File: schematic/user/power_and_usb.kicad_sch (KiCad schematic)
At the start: 39 parts, among them J1 TYPE-C-31-M-04, Q1 AO3401A, Q2 AO3401A, Q5 MBT3904DW1T1, U1 TP4056, U2 MAX17048G+T10, U3 NCP167AFCT330T2G, U6 ESD122DMXR

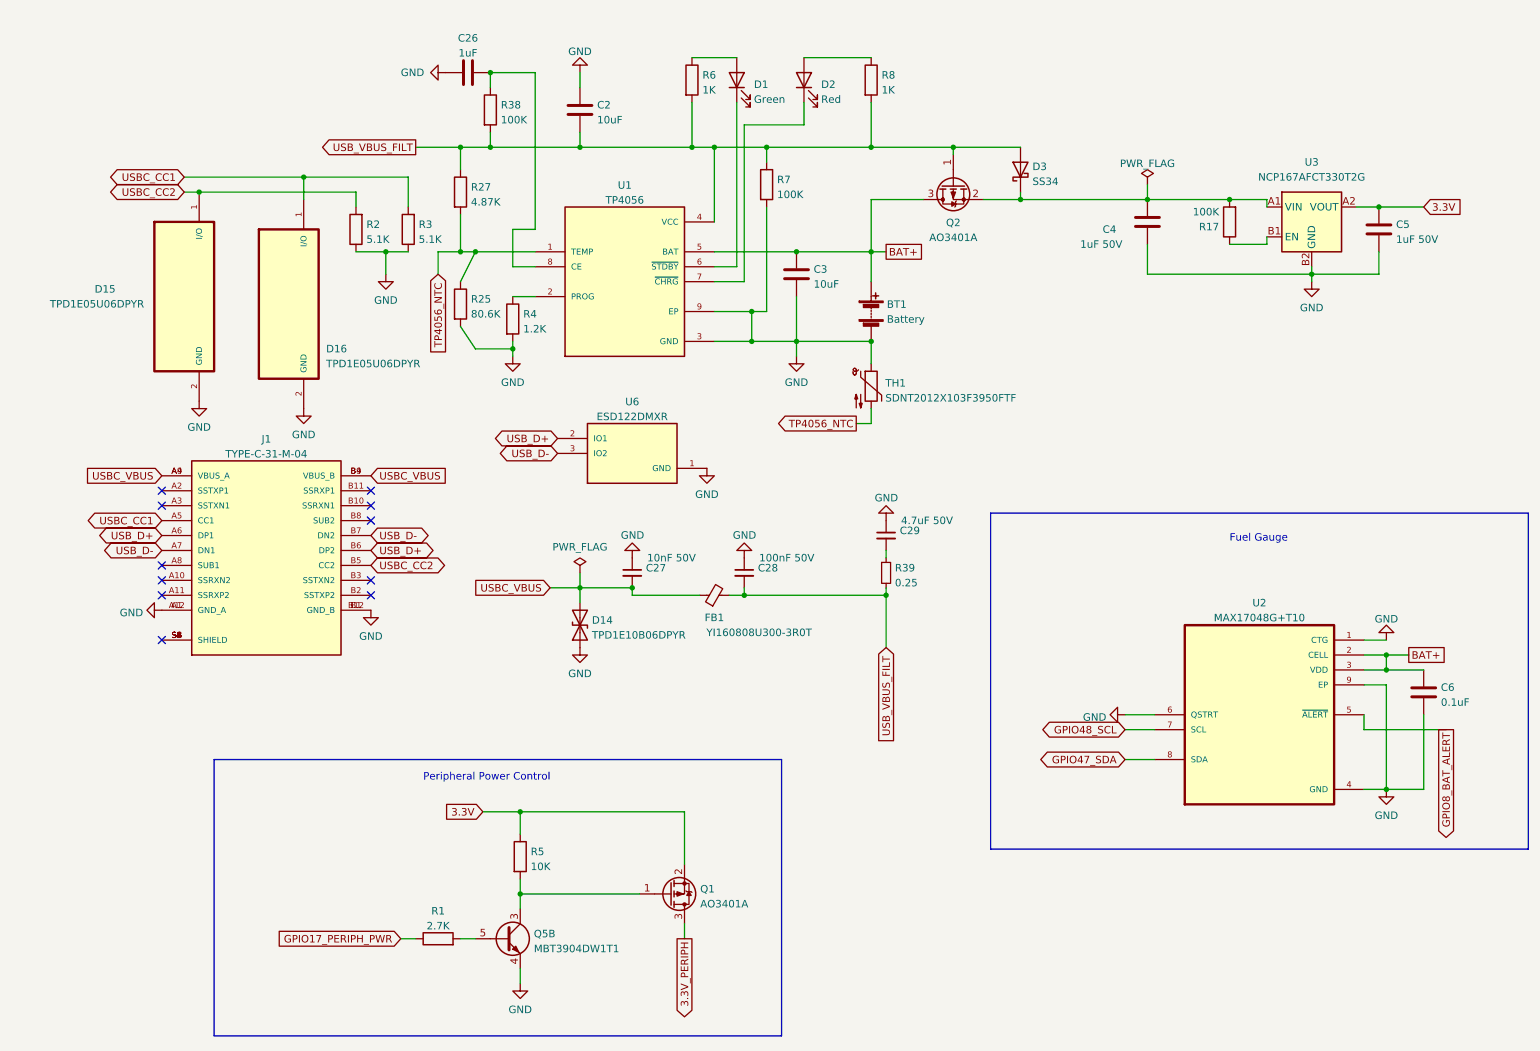
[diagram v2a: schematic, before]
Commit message: v0.7 board: resolve all ERC errors in schematic.
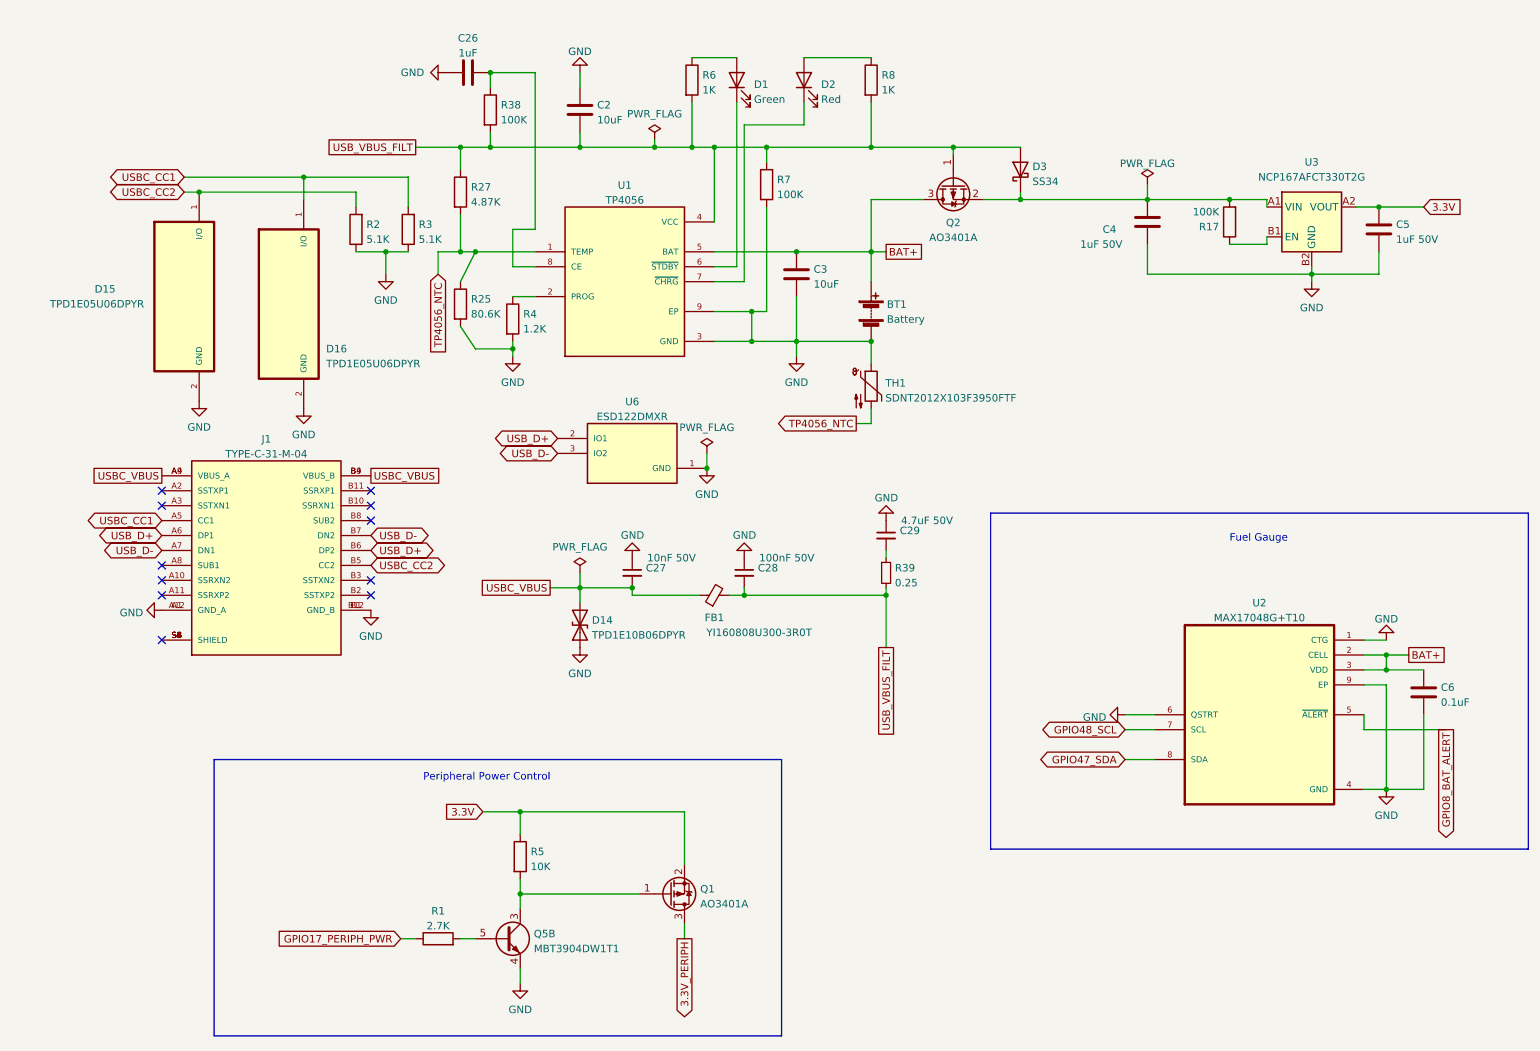
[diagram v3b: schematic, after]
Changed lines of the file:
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@@
   (junction (at 254 144.78) (diameter 0) (color 0 0 0 0)
   )
+  (junction (at 138.43 90.17) (diameter 0) (color 0 0 0 0)
+  )
   (junction (at 153.67 68.58) (diameter 0) (color 0 0 0 0)
   )
@@
   )
   (junction (at 191.77 44.45) (diameter 0) (color 0 0 0 0)
+  )
+  (junction (at 129.54 35.56) (diameter 0) (color 0 0 0 0)
   )
   (junction (at 146.05 63.5) (diameter 0) (color 0 0 0 0)
@@
     (stroke (width 0) (type default) (color 0 0 0 0))
   )
+  (wire (pts (xy 166.37 53.34) (xy 166.37 58.42))
+    (stroke (width 0) (type default) (color 0 0 0 0))
+  )
   (wire (pts (xy 105.41 49.53) (xy 105.41 55.88))
     (stroke (width 0) (type default) (color 0 0 0 0))
@@
     (stroke (width 0) (type default) (color 0 0 0 0))
   )
-  (wire (pts (xy 116.84 35.56) (xy 135.89 35.56))
+  (wire (pts (xy 116.84 35.56) (xy 129.54 35.56))
     (stroke (width 0) (type default) (color 0 0 0 0))
   )
@@
     (stroke (width 0) (type default) (color 0 0 0 0))
   )
-  (wire (pts (xy 166.37 53.34) (xy 166.37 58.42))
-    (stroke (width 0) (type default) (color 0 0 0 0))
-  )
   (wire (pts (xy 153.67 68.58) (xy 153.67 60.96))
     (stroke (width 0) (type default) (color 0 0 0 0))
@@
     (stroke (width 0) (type default) (color 0 0 0 0))
   )
+  (wire (pts (xy 129.54 34.29) (xy 129.54 35.56))
+    (stroke (width 0) (type default) (color 0 0 0 0))
+  )
   (wire (pts (xy 49.53 40.64) (xy 69.85 40.64))
     (stroke (width 0) (type default) (color 0 0 0 0))
@@
     (stroke (width 0) (type default) (color 0 0 0 0))
   )
+  (wire (pts (xy 138.43 87.63) (xy 138.43 90.17))
+    (stroke (width 0) (type default) (color 0 0 0 0))
+  )
   (wire (pts (xy 254 144.78) (xy 260.35 144.78))
     (stroke (width 0) (type default) (color 0 0 0 0))
@@
   )
   (wire (pts (xy 166.37 27.94) (xy 166.37 35.56))
+    (stroke (width 0) (type default) (color 0 0 0 0))
+  )
+  (wire (pts (xy 129.54 35.56) (xy 135.89 35.56))
     (stroke (width 0) (type default) (color 0 0 0 0))
   )
@@
     )
   )
-  (global_label "USBC_VBUS" (shape input) (at 81.28 91.44 0) (fields_autoplaced)
+  (global_label "USBC_VBUS" (shape passive) (at 81.28 91.44 0) (fields_autoplaced)
     (effects (font (size 1.27 1.27)) (justify left))
     (property "Intersheet References" "${INTERSHEET_REFS}" (id 0) (at 94.6393 91.3606 0)
@@
     )
   )
-  (global_label "USBC_VBUS" (shape input) (at 111.76 110.49 180) (fields_autoplaced)
-    (effects (font (size 1.27 1.27)) (justify right))
-    (property "Intersheet References" "${INTERSHEET_REFS}" (id 0) (at 98.4007 110.5694 0)
-      (effects (font (size 1.27 1.27)) (justify right) hide)
-    )
-  )
-  (global_label "USB_VBUS_FILT" (shape input) (at 168.91 120.65 270) (fields_autoplaced)
-    (effects (font (size 1.27 1.27)) (justify right))
-    (property "Intersheet References" "${INTERSHEET_REFS}" (id 0) (at 168.9894 137.396 90)
+  (global_label "USBC_VBUS" (shape passive) (at 111.76 110.49 180) (fields_autoplaced)
+    (effects (font (size 1.27 1.27)) (justify right))
+    (property "Intersheet References" "${INTERSHEET_REFS}" (id 0) (at 98.4007 110.4106 0)
+      (effects (font (size 1.27 1.27)) (justify right) hide)
+    )
+  )
+  (global_label "USB_VBUS_FILT" (shape passive) (at 168.91 120.65 270) (fields_autoplaced)
+    (effects (font (size 1.27 1.27)) (justify right))
+    (property "Intersheet References" "${INTERSHEET_REFS}" (id 0) (at 168.8306 137.396 90)
       (effects (font (size 1.27 1.27)) (justify right) hide)
     )
@@
     )
   )
-  (global_label "USB_VBUS_FILT" (shape output) (at 88.9 35.56 180) (fields_autoplaced)
+  (global_label "USB_VBUS_FILT" (shape passive) (at 88.9 35.56 180) (fields_autoplaced)
     (effects (font (size 1.27 1.27)) (justify right))
     (property "Intersheet References" "${INTERSHEET_REFS}" (id 0) (at 72.154 35.4806 0)
@@
     )
   )
-  (global_label "USBC_VBUS" (shape input) (at 45.72 91.44 180) (fields_autoplaced)
-    (effects (font (size 1.27 1.27)) (justify right))
-    (property "Intersheet References" "${INTERSHEET_REFS}" (id 0) (at 32.3607 91.5194 0)
+  (global_label "USBC_VBUS" (shape passive) (at 45.72 91.44 180) (fields_autoplaced)
+    (effects (font (size 1.27 1.27)) (justify right))
+    (property "Intersheet References" "${INTERSHEET_REFS}" (id 0) (at 32.3607 91.3606 0)
       (effects (font (size 1.27 1.27)) (justify right) hide)
     )
@@
       (effects (font (size 1.27 1.27)) (justify left) hide)
     )
+  )
+  (symbol (lib_id "power:PWR_FLAG") (at 129.54 34.29 0) (unit 1)
+    (in_bom yes) (on_board yes)
+    (property "Reference" "#FLG0101" (id 0) (at 129.54 32.385 0)
+      (effects (font (size 1.27 1.27)) hide)
+    )
+    (property "Value" "PWR_FLAG" (id 1) (at 129.54 29.8958 0))
+    (property "Footprint" "" (id 2) (at 129.54 34.29 0)
+      (effects (font (size 1.27 1.27)) hide)
+    )
+    (property "Datasheet" "~" (id 3) (at 129.54 34.29 0)
+      (effects (font (size 1.27 1.27)) hide)
+    )
+    (pin "1")
   )
   (symbol (lib_id "Device:C_Small") (at 168.91 101.6 0) (unit 1)
@@
     (pin "2")
   )
+  (symbol (lib_id "power:PWR_FLAG") (at 138.43 87.63 0) (unit 1)
+    (in_bom yes) (on_board yes)
+    (property "Reference" "#FLG0102" (id 0) (at 138.43 85.725 0)
+      (effects (font (size 1.27 1.27)) hide)
+    )
+    (property "Value" "PWR_FLAG" (id 1) (at 138.43 83.2358 0))
+    (property "Footprint" "" (id 2) (at 138.43 87.63 0)
+      (effects (font (size 1.27 1.27)) hide)
+    )
+    (property "Datasheet" "~" (id 3) (at 138.43 87.63 0)
+      (effects (font (size 1.27 1.27)) hide)
+    )
+    (pin "1")
+  )
   (symbol (lib_id "power:GND") (at 153.67 71.12 0) (unit 1)

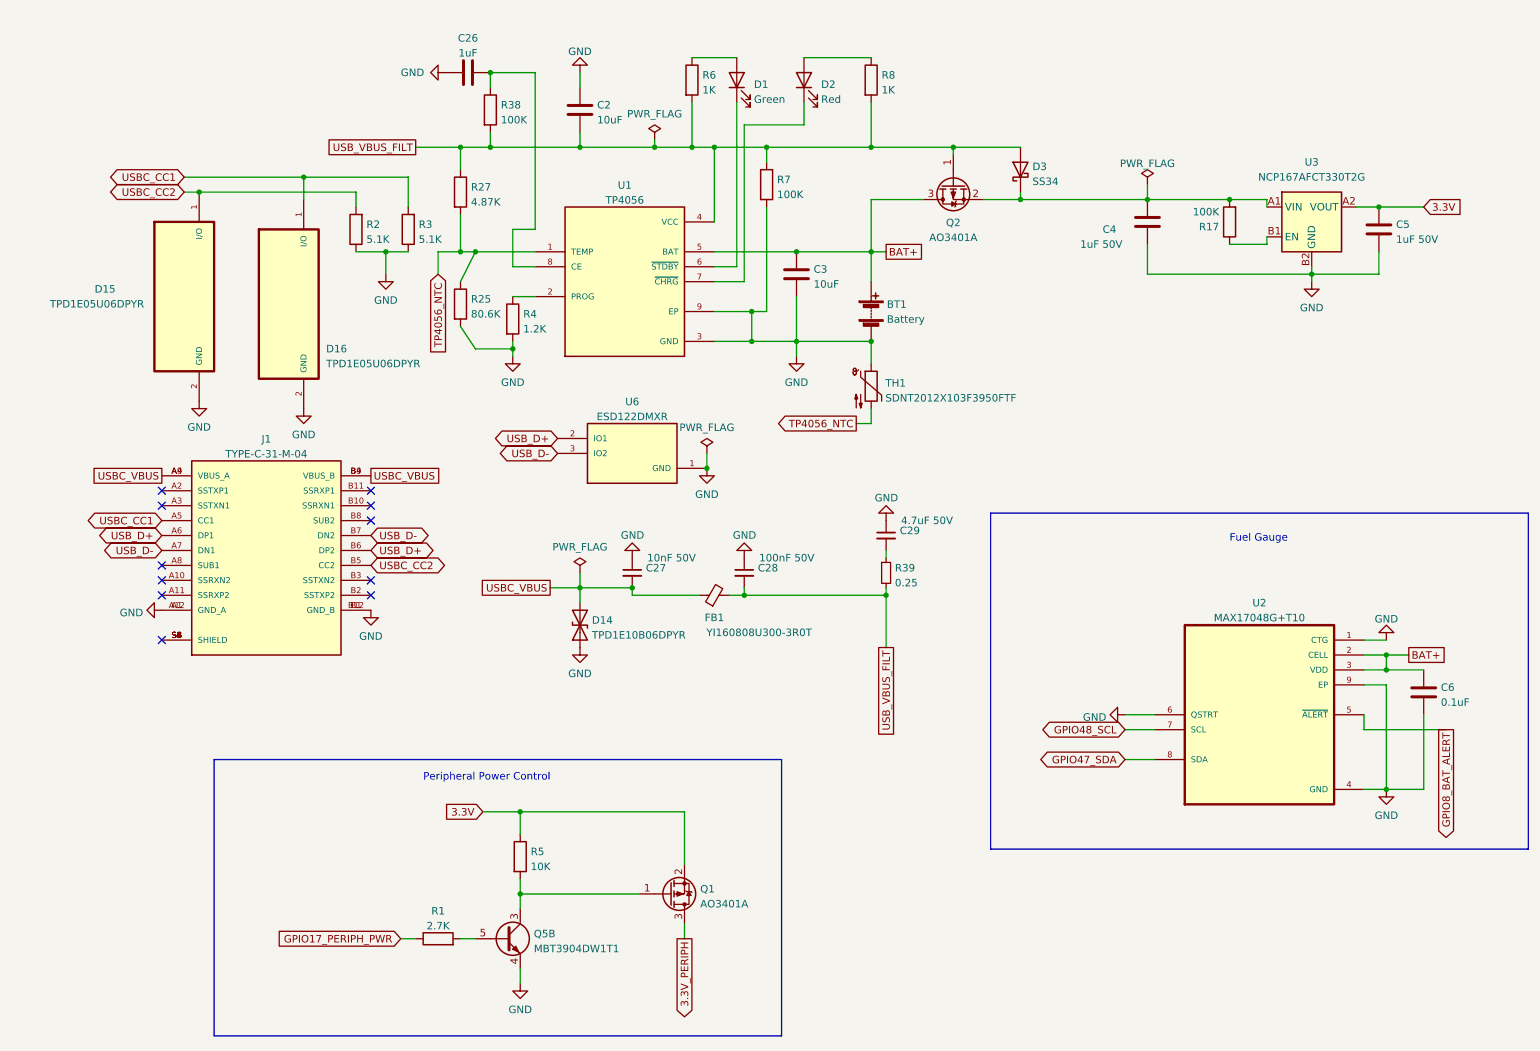
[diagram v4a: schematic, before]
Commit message: v0.7 board: add WUSB3801 and reduce TP4056 max current if USB port doesn't support >=1.5A current.
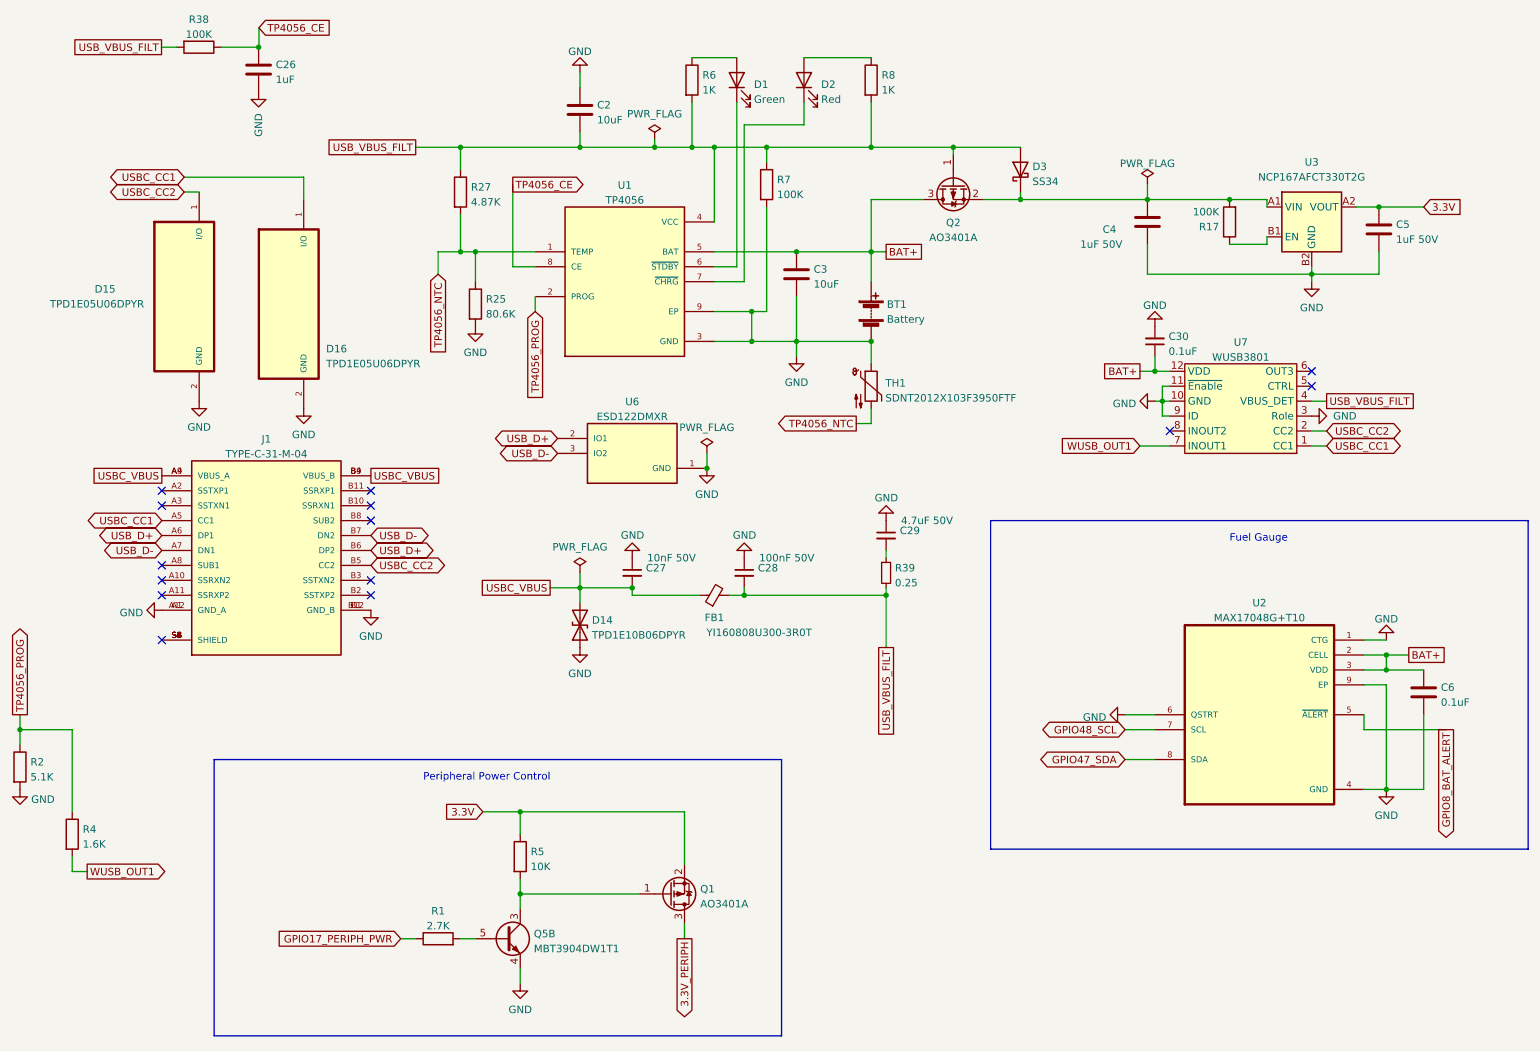
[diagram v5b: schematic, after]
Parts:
- removed R3: 5.1K, Resistor_SMD:R_0402_1005Metric, symbol Device:R
- added C30: 0.1uF, Capacitor_SMD:C_0402_1005Metric, symbol Device:C_Small
- added U7: WUSB3801, ezDV_production:QFN1616-12L, symbol ezDV-rescue:WUSB3801
- R4: value 1.2K -> 1.6K; LCSC C25862 -> C4908
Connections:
- net BAT+: now also C30.1, U7.12 (VDD)
- net GND: now also R2.2, C30.2, U7.10 (GND), U7.11 (~{Enable}), U7.3 (Role), U7.9 (ID); no longer R2.1, R4.2
- net USBC_CC1: now also U7.1 (CC1)
- net USBC_CC2: now also U7.2 (CC2); no longer R2.2
- net USB_VBUS_FILT: now also U7.4 (VBUS_DET)
- net TP4056_CE: now reaches C26.2, R38.1, U1.8 (CE)
- net TP4056_PROG: now reaches R4.1, U1.2 (PROG)
- net TP4056_PROG: now also R2.1
- new net WUSB_OUT1: R4.2, U7.7 (INOUT1)
- no-connect marks 11 -> 14
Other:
- moved on the sheet: C26, R25, R38, R4
